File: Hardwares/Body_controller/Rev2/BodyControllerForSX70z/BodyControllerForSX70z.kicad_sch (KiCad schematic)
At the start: 26 parts, among them J1 Conn_01x06_Socket, J2 Conn_01x03_Socket, U3 PCF8574ATS

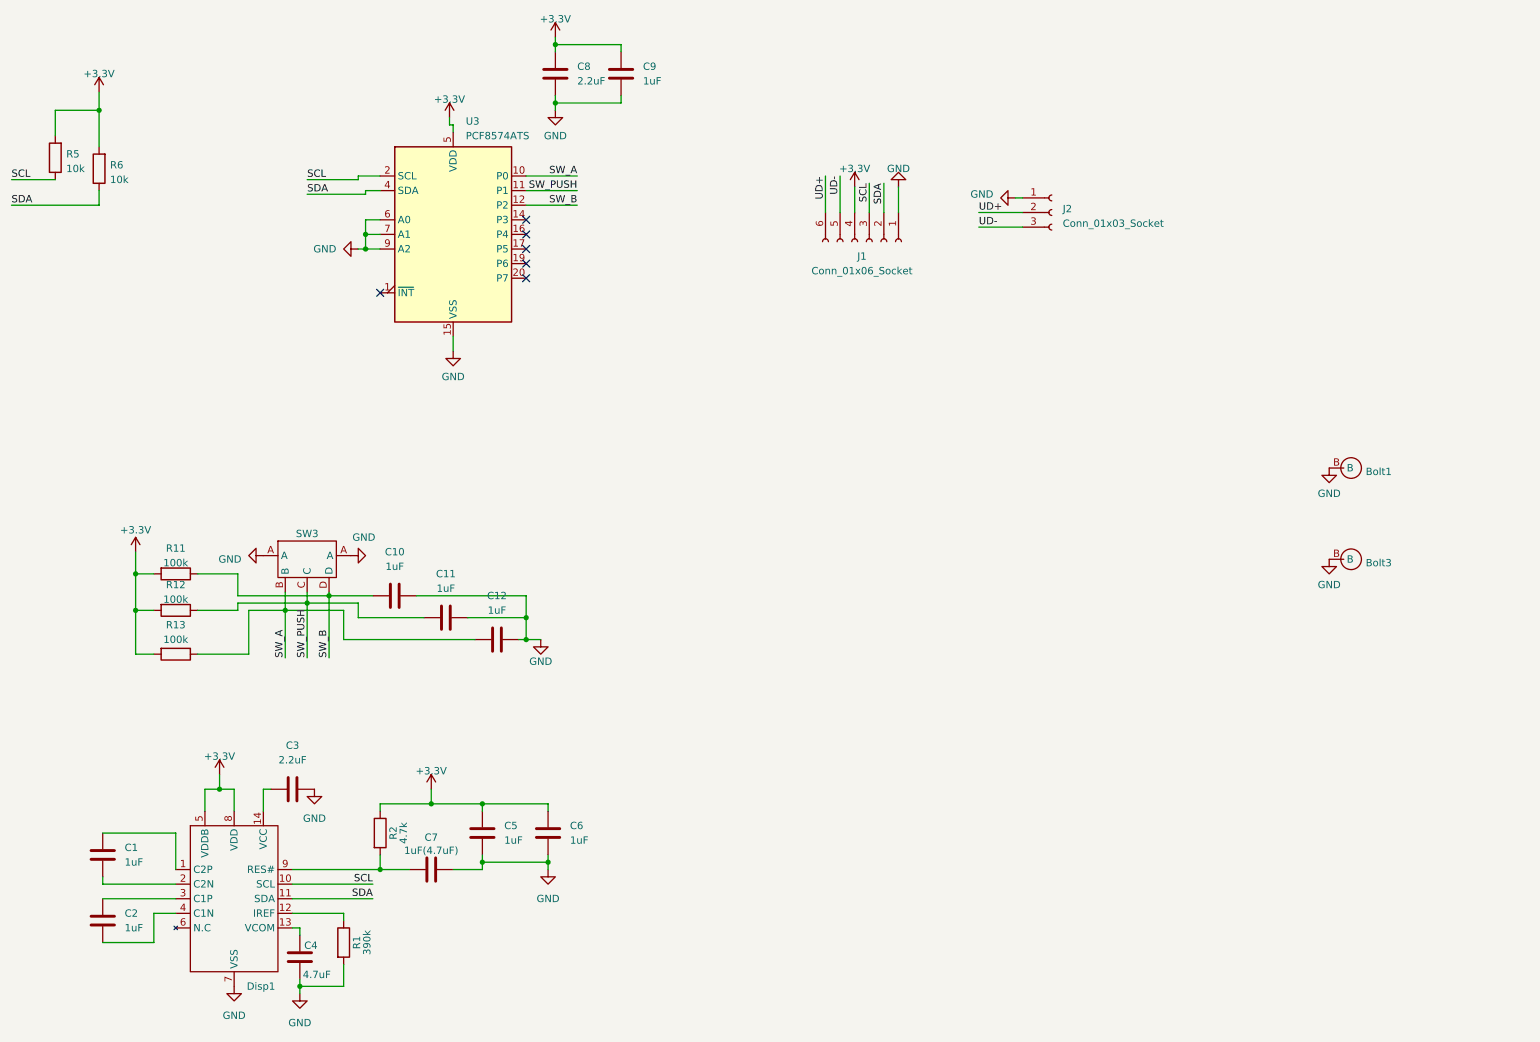
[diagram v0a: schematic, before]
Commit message: 修改SX70zPCB的小问题，投产机身控制器
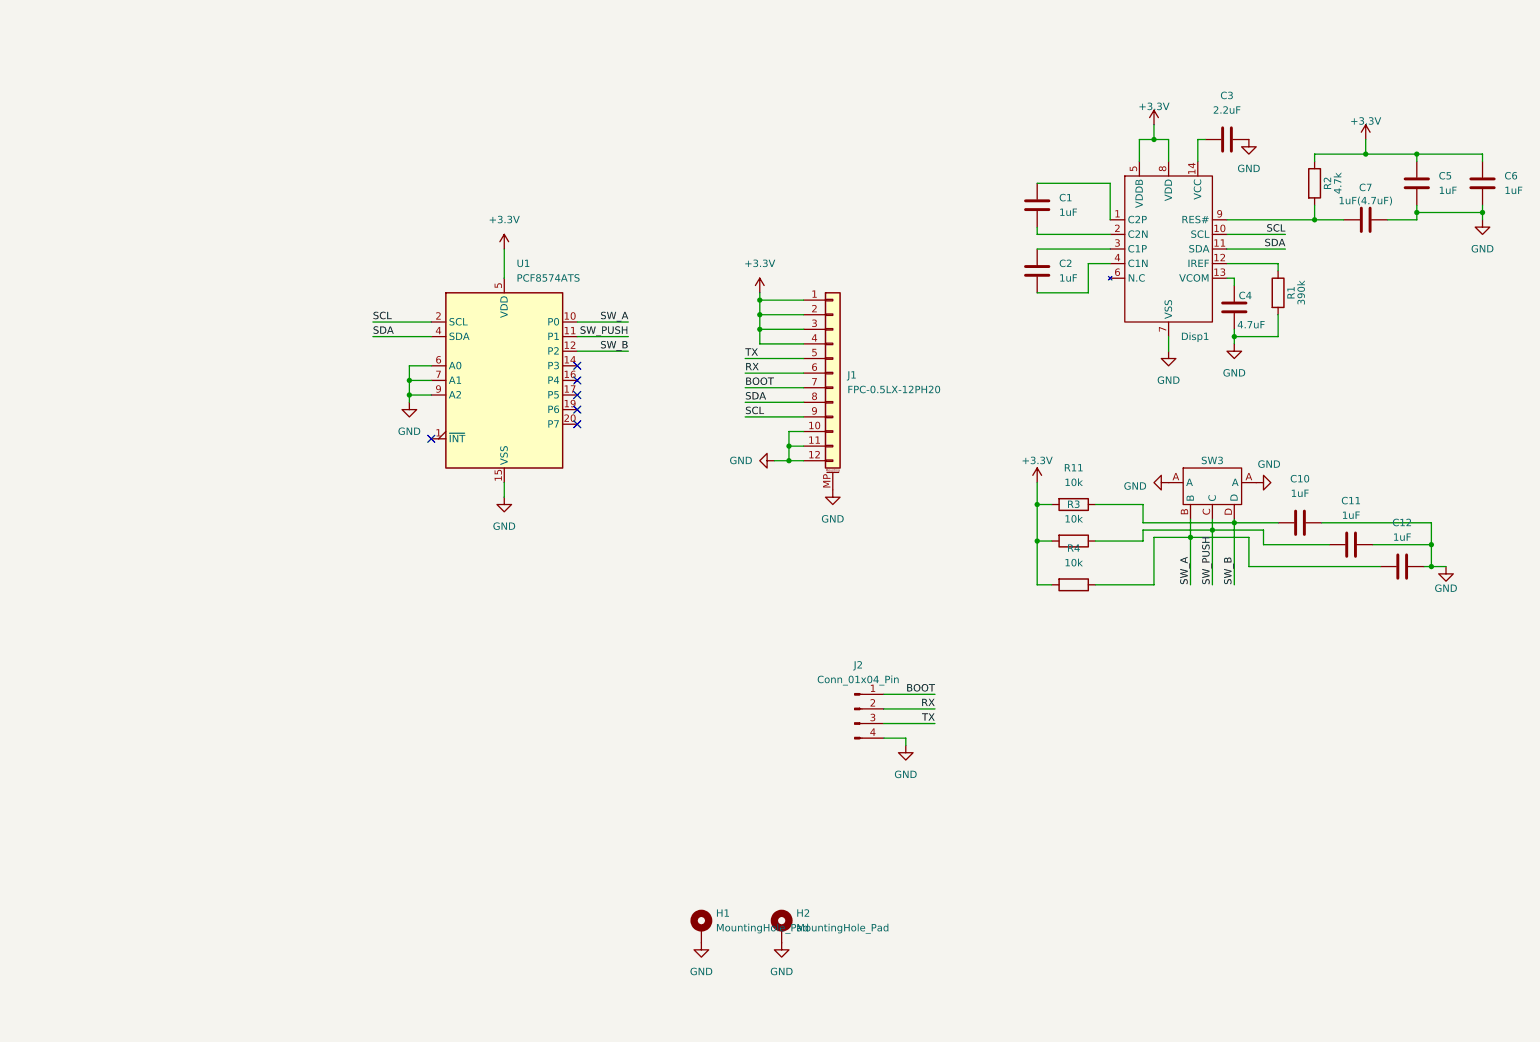
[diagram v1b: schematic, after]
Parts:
- removed Bolt1, Bolt3: ~, 0JIMMY:M3_Bolt, symbol 0JIMMY:M3_Bolt
- removed C8: 2.2uF, Capacitor_SMD:C_0603_1608Metric_Pad1.08x0.95mm_HandSolder, symbol Device:C
- removed C9: 1uF, Capacitor_SMD:C_0603_1608Metric_Pad1.08x0.95mm_HandSolder, symbol Device:C
- removed J1: Conn_01x06_Socket, Connector_FFC-FPC:TE_84953-6_1x06-1MP_P1.0mm_Horizontal, symbol Connector:Conn_01x06_Socket
- removed J2: Conn_01x03_Socket, Connector_PinHeader_2.54mm:PinHeader_1x03_P2.54mm_Horizontal, symbol Connector:Conn_01x03_Socket
- removed R12, R13: 100k, Resistor_SMD:R_0603_1608Metric_Pad0.98x0.95mm_HandSolder, symbol Device:R
- removed R5, R6: 10k, Resistor_SMD:R_0805_2012Metric_Pad1.20x1.40mm_HandSolder, symbol Device:R
- removed U3: PCF8574ATS, Package_SO:SSOP-20_4.4x6.5mm_P0.65mm, symbol Interface_Expansion:PCF8574ATS
- added H1, H2: MountingHole_Pad, MountingHole:MountingHole_3.2mm_M3_DIN965_Pad, symbol Mechanical:MountingHole_Pad
- added J1: FPC-0.5LX-12PH20, KiCadLib:FPC-0.5LX-12PH20, symbol Connector_Generic_MountingPin:Conn_01x12_MountingPin
- added J2: Conn_01x04_Pin, Connector_PinHeader_2.54mm:PinHeader_1x04_P2.54mm_Horizontal, symbol Connector:Conn_01x04_Pin
- added R3, R4: 10k, Resistor_SMD:R_0603_1608Metric_Pad0.98x0.95mm_HandSolder, symbol Device:R
- added U1: PCF8574ATS, Package_SO:SSOP-20_4.4x6.5mm_P0.65mm, symbol Interface_Expansion:PCF8574ATS
- R11: value 100k -> 10k
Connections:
- net +3.3V: now also J1.1 (Pin_1), J1.2 (Pin_2), J1.3 (Pin_3), J1.4 (Pin_4), R3.2, R4.2, U1.5 (VDD)
- net GND: now also H1.1, H2.1, J1.10 (Pin_10), J1.11 (Pin_11), J1.12 (Pin_12), J1.MP (MountPin), J2.4 (Pin_4), U1.15 (VSS), U1.6 (A0), U1.7 (A1), U1.9 (A2)
- net SCL: now also J1.9 (Pin_9), U1.2 (SCL)
- net SDA: now also J1.8 (Pin_8), U1.4 (SDA)
- net SW_A: now also R4.1, U1.10 (P0)
- net SW_B: now also U1.12 (P2)
- net SW_PUSH: now also R3.1, U1.11 (P1)
- new net BOOT: J1.7 (Pin_7), J2.1 (Pin_1)
- new net RX: J1.6 (Pin_6), J2.2 (Pin_2)
- new net TX: J1.5 (Pin_5), J2.3 (Pin_3)
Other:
- title: (none) -> SX70 Model Z 机身控制器
- moved on the sheet: C1, C10, C11, C12, C2, C3, C4, C5, C6, C7, R1, R11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
